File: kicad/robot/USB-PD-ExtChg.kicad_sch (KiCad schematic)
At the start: 32 parts, among them J1 USBC_Receptacle_SMD_RA, Q3 YJL3416A, Q4 YJL3416A, U18 AP33771DKZ-13, U25 TVS0500DRV, U26 TPD1E05U06, U27 TPD1E05U06, U28 TPD1E05U06, U29 TPD1E05U06

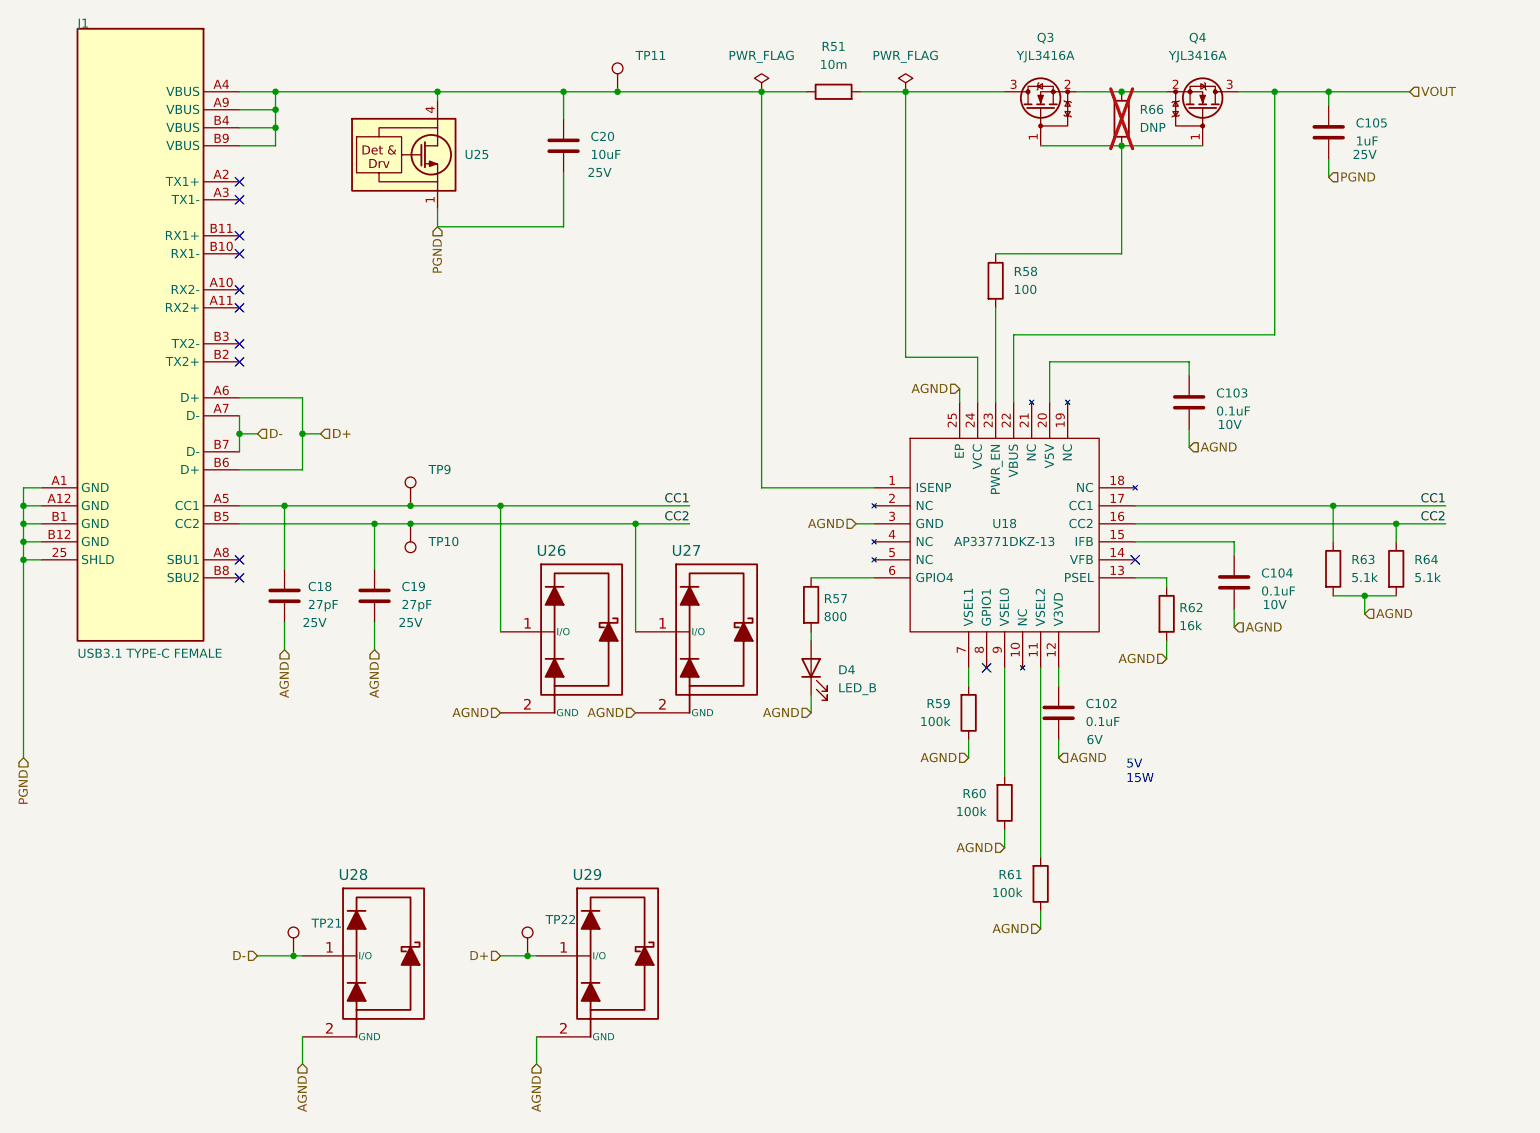
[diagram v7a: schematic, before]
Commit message: Replaced all test points with SMD parts where possible
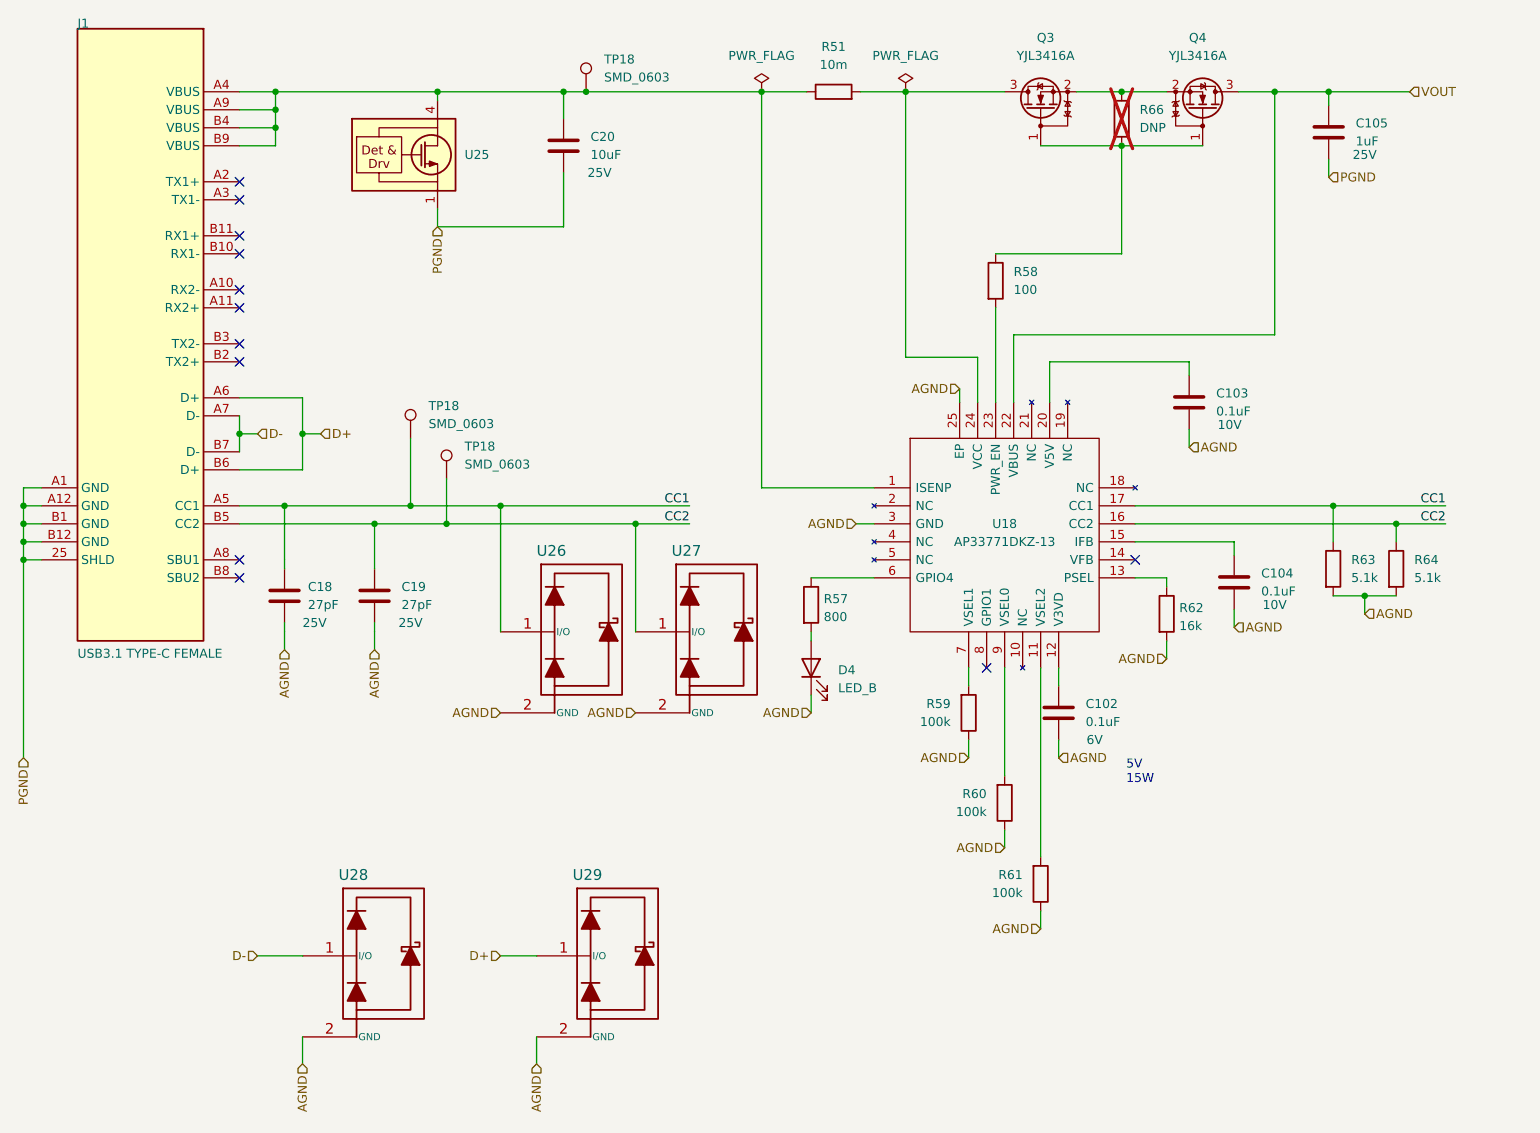
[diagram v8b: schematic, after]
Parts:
- removed TP10, TP11, TP21, TP22, TP9: TestPoint, robot:KEYSTONE_5002, symbol robot:TestPoint
- added TP18 (x3): SMD_0603, robot:TestPoint_SMD_0603, symbol robot:TestPoint
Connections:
- net CC1: now also TP18.1
- net CC2: now also TP18.1
- net at C20.1, J1.A4 (VBUS), J1.A9 (VBUS)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: now also TP18.1
